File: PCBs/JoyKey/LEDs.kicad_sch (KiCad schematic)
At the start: 5 parts

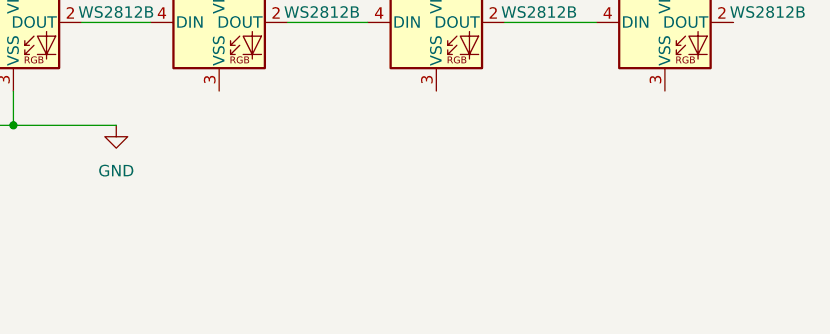
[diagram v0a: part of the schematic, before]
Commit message: Add draft schematics for all the input sources
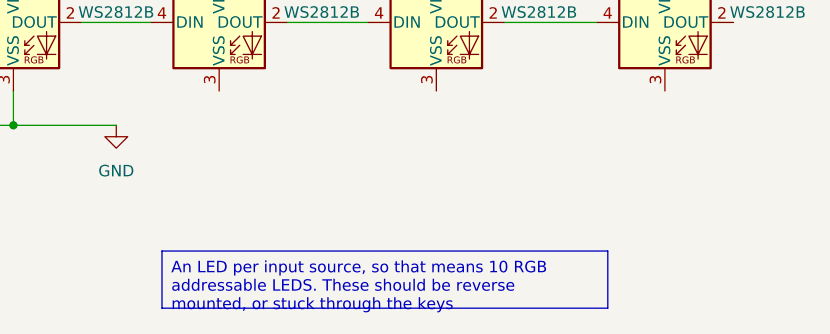
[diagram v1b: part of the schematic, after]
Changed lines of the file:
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@@
+		)
+	)
+	(text_box "An LED per input source, so that means 10 RGB addressable LEDS. These should be reverse mounted, or stuck through the keys"
+		(exclude_from_sim no)
+		(at 81.28 80.01 0)
+		(size 49.53 6.35)
+		(stroke
+			(width 0)
+			(type default)
+		)
+		(fill
+			(type none)
+		)
+		(effects
+			(font
+				(size 1.27 1.27)
+			)
+			(justify left top)
 		)
 	)

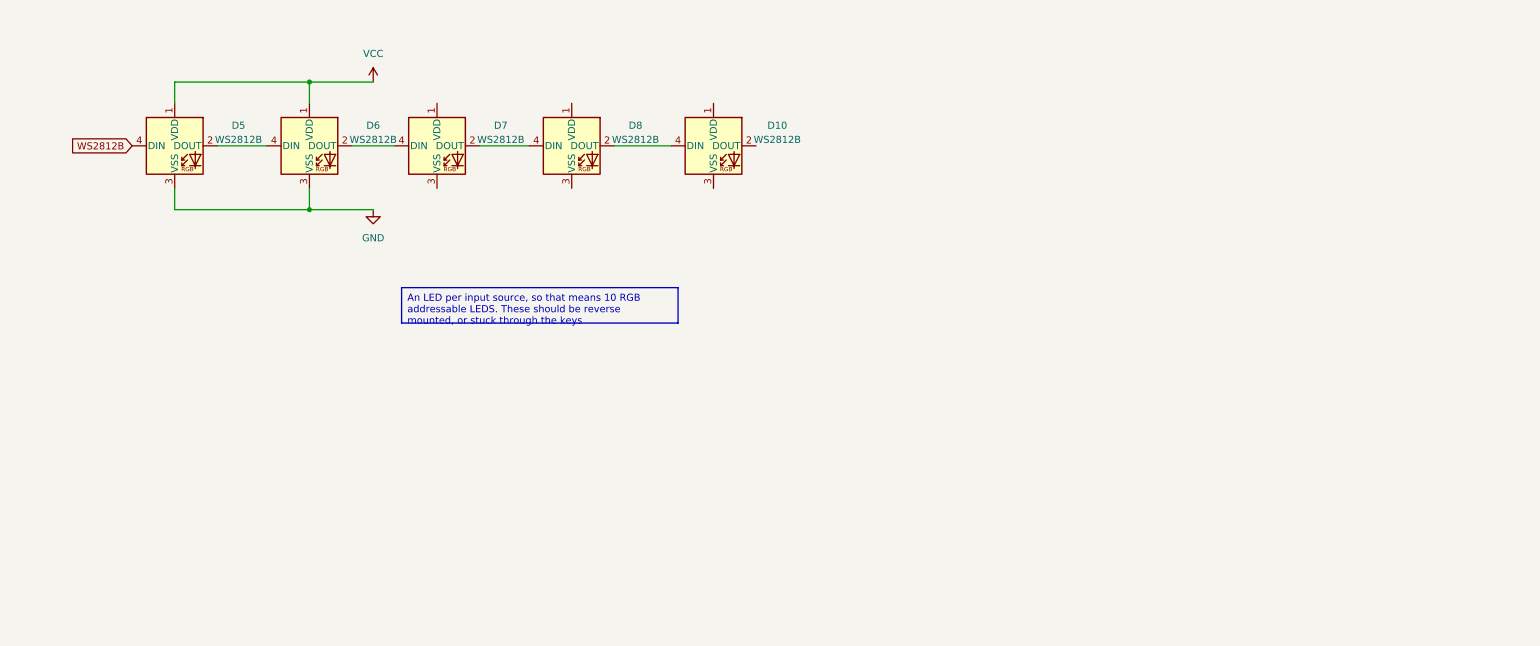
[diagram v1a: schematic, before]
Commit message: Rearranged LEDs and switched to SK6812 mini -e
These are reverse mount RGB LEDs that I think would be better to use than the ws2812 leds
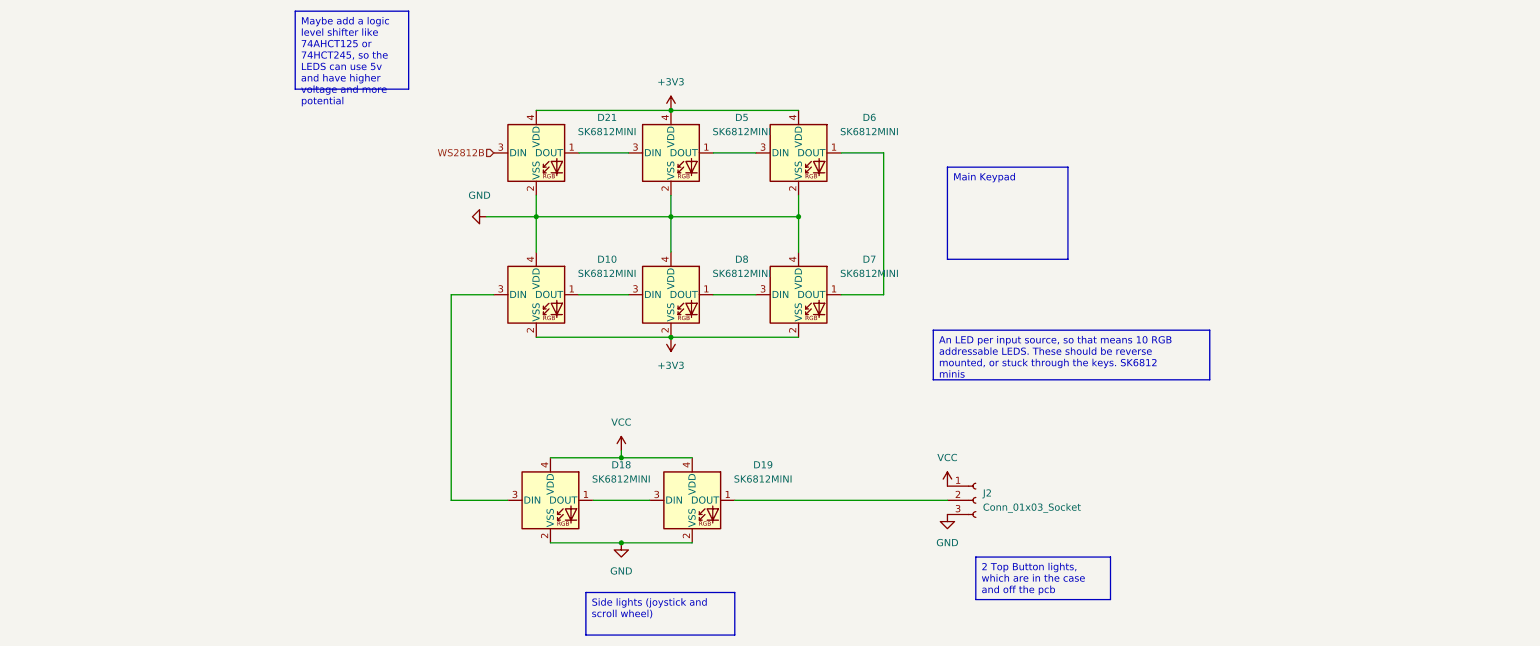
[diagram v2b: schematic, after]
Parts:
- removed D10, D5, D6, D7, D8: WS2812B, LED_SMD:LED_WS2812B_PLCC4_5.0x5.0mm_P3.2mm, symbol LED:WS2812B
- added D10, D18, D19, D21, D5, D6, D7, D8: SK6812MINI, SK6812MINI-E:SK6812MINI-E, symbol LED:SK6812MINI
- added J2: Conn_01x03_Socket, Connector_PinHeader_2.54mm:PinHeader_1x03_P2.54mm_Vertical, symbol Connector:Conn_01x03_Socket
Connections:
- net GND: now also D10.4 (VDD), D18.2 (VSS), D19.2 (VSS), D21.2 (VSS), D5.2 (VSS), D6.2 (VSS), D7.4 (VDD), D8.4 (VDD), J2.3 (Pin_3)
- net VCC: now also D18.4 (VDD), D19.4 (VDD), J2.1 (Pin_1)
- net WS2812B: now also D21.3 (DIN)
- new net: D21.1 (DOUT), D5.3 (DIN)
- new net: D18.1 (DOUT), D19.3 (DIN)
- new net: D10.3 (DIN), D18.3 (DIN)
- new net: D19.1 (DOUT), J2.2 (Pin_2)
- new net: D6.1 (DOUT), D7.1 (DOUT)
- new net: D5.1 (DOUT), D6.3 (DIN)
- new net: D7.3 (DIN), D8.1 (DOUT)
- new net: D10.1 (DOUT), D8.3 (DIN)
- new net +3V3: D10.2 (VSS), D21.4 (VDD), D5.4 (VDD), D6.4 (VDD), D7.2 (VSS), D8.2 (VSS)

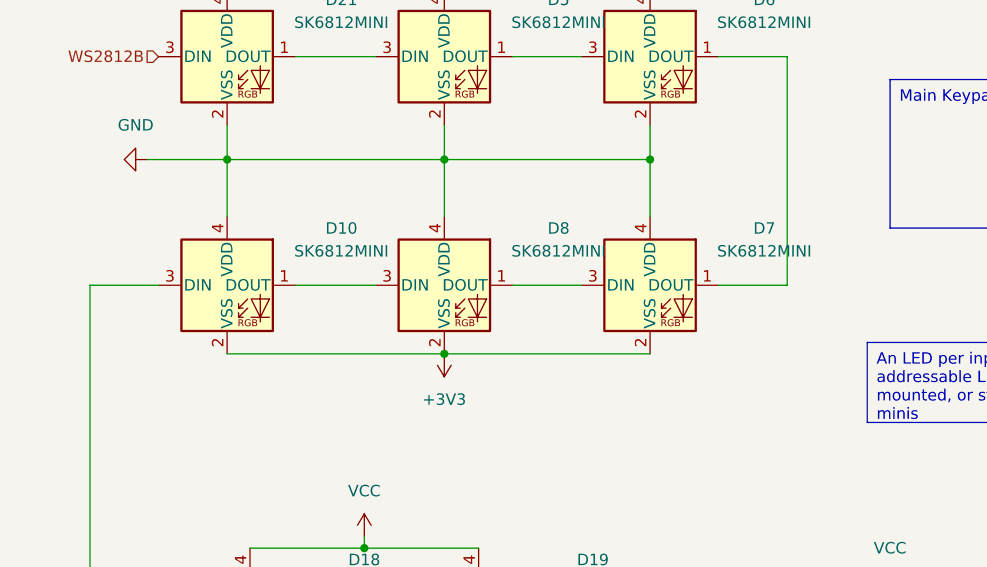
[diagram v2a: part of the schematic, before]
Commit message: Fixed bug w reverse orientation of LEDs
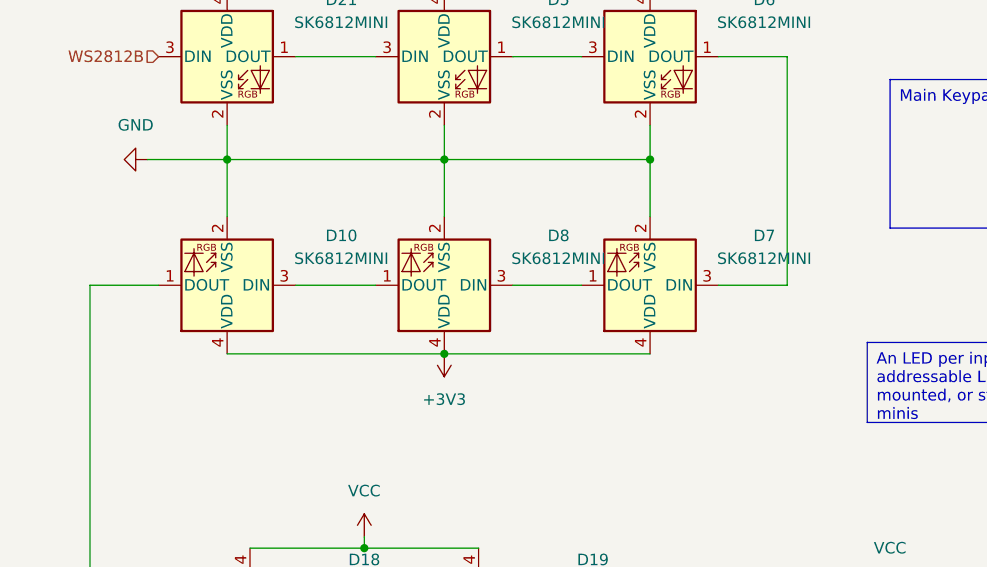
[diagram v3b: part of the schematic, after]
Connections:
- net +3V3: now also D10.4 (VDD), D7.4 (VDD), D8.4 (VDD); no longer D10.2 (VSS), D7.2 (VSS), D8.2 (VSS)
- net GND: now also D10.2 (VSS), D7.2 (VSS), D8.2 (VSS); no longer D10.4 (VDD), D7.4 (VDD), D8.4 (VDD)
- net at D18.3 (DIN): now also D10.1 (DOUT); no longer D10.3 (DIN)
- net at D6.1 (DOUT): now also D7.3 (DIN); no longer D7.1 (DOUT)
- net at D8.1 (DOUT): now also D10.3 (DIN); no longer D7.3 (DIN)
- net at D8.3 (DIN): now also D7.1 (DOUT); no longer D10.1 (DOUT)
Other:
- moved on the sheet: D10, D7, D8
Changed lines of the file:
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@@
 	(symbol
 		(lib_id "LED:SK6812MINI")
-		(at 129.54 81.28 0)
+		(at 129.54 81.28 180)
 		(unit 1)
 		(exclude_from_sim no)
@@
 		(fields_autoplaced yes)
 		(property "Reference" "D8"
-			(at 142.24 74.9614 0)
+			(at 142.24 75.7838 0)
 			(effects
 				(font
@@
 		)
 		(property "Value" "SK6812MINI"
-			(at 142.24 77.5014 0)
+			(at 142.24 78.3238 0)
 			(effects
 				(font
@@
 		)
 		(property "Footprint" "SK6812MINI-E:SK6812MINI-E"
-			(at 130.81 88.9 0)
+			(at 128.27 73.66 0)
 			(effects
 				(font
@@
 		)
 		(property "Datasheet" "https://cdn-shop.adafruit.com/product-files/2686/SK6812MINI_REV.01-1-2.pdf"
-			(at 132.08 90.805 0)
+			(at 127 71.755 0)
 			(effects
 				(font
@@
 	(symbol
 		(lib_id "LED:SK6812MINI")
-		(at 152.4 81.28 0)
+		(at 152.4 81.28 180)
 		(unit 1)
 		(exclude_from_sim no)
@@
 		(fields_autoplaced yes)
 		(property "Reference" "D7"
-			(at 165.1 74.9614 0)
+			(at 165.1 75.7838 0)
 			(effects
 				(font
@@
 		)
 		(property "Value" "SK6812MINI"
-			(at 165.1 77.5014 0)
+			(at 165.1 78.3238 0)
 			(effects
 				(font
@@
 		)
 		(property "Footprint" "SK6812MINI-E:SK6812MINI-E"
-			(at 153.67 88.9 0)
+			(at 151.13 73.66 0)
 			(effects
 				(font
@@
 		)
 		(property "Datasheet" "https://cdn-shop.adafruit.com/product-files/2686/SK6812MINI_REV.01-1-2.pdf"
-			(at 154.94 90.805 0)
+			(at 149.86 71.755 0)
 			(effects
 				(font
@@
 	(symbol
 		(lib_id "LED:SK6812MINI")
-		(at 105.41 81.28 0)
+		(at 105.41 81.28 180)
 		(unit 1)
 		(exclude_from_sim no)
@@
 		(fields_autoplaced yes)
 		(property "Reference" "D10"
-			(at 118.11 74.9614 0)
+			(at 118.11 75.7838 0)
 			(effects
 				(font
@@
 		)
 		(property "Value" "SK6812MINI"
-			(at 118.11 77.5014 0)
+			(at 118.11 78.3238 0)
 			(effects
 				(font
@@
 		)
 		(property "Footprint" "SK6812MINI-E:SK6812MINI-E"
-			(at 106.68 88.9 0)
+			(at 104.14 73.66 0)
 			(effects
 				(font
@@
 		)
 		(property "Datasheet" "https://cdn-shop.adafruit.com/product-files/2686/SK6812MINI_REV.01-1-2.pdf"
-			(at 107.95 90.805 0)
-			(effects
-				(font
+			(at 102.87 71.755 0)
+			(effects
+				(font

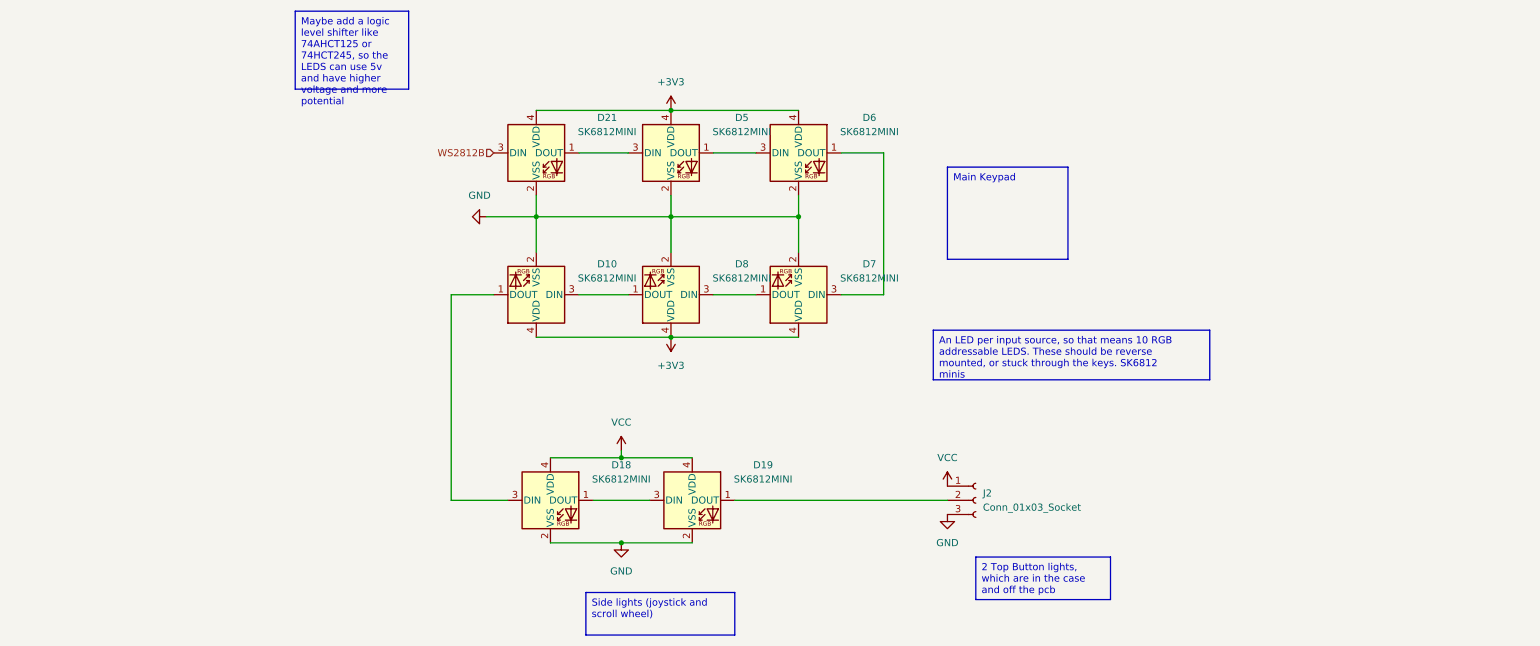
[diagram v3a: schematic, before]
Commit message: Updated to not distinguished btw LEDs per element
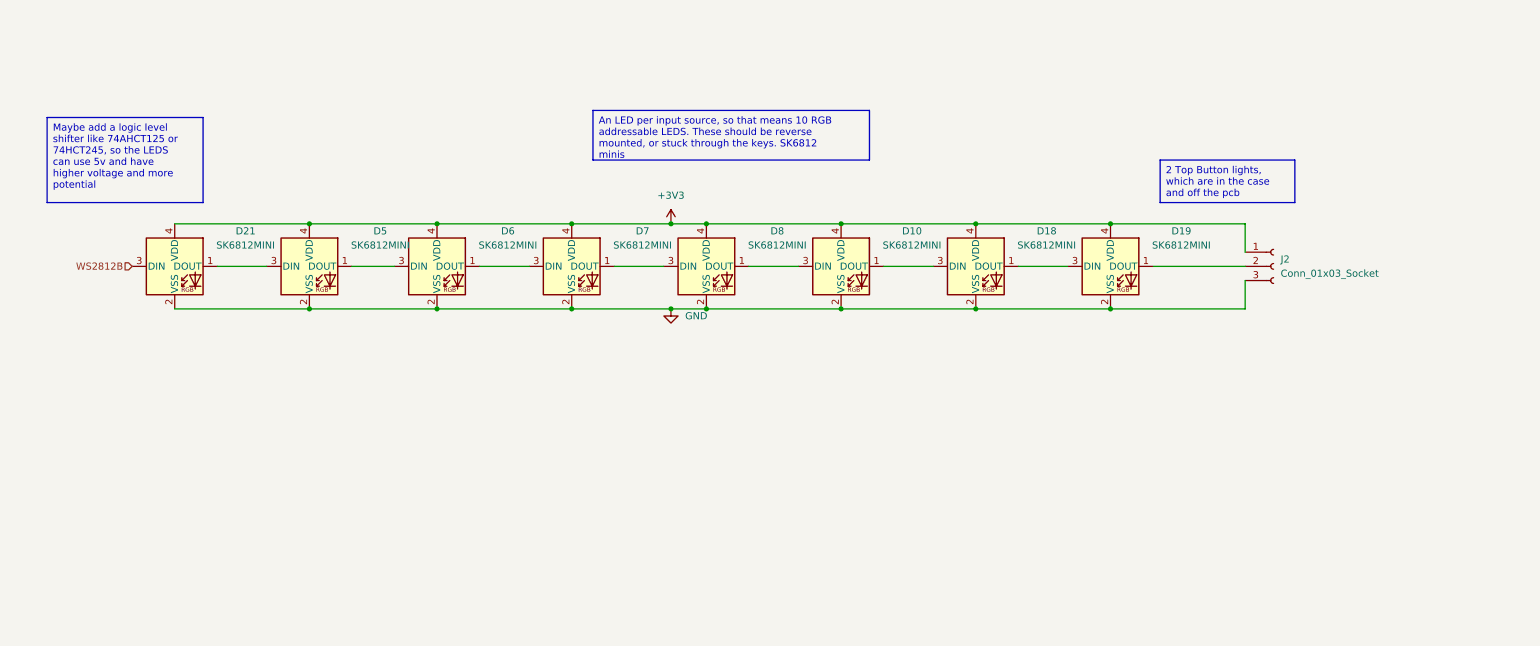
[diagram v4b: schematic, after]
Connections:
- net VCC is gone; now on net +3V3: D18.4 (VDD), D19.4 (VDD), J2.1 (Pin_1)
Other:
- moved on the sheet: D10, D18, D19, D21, D5, D6, D7, D8, J2

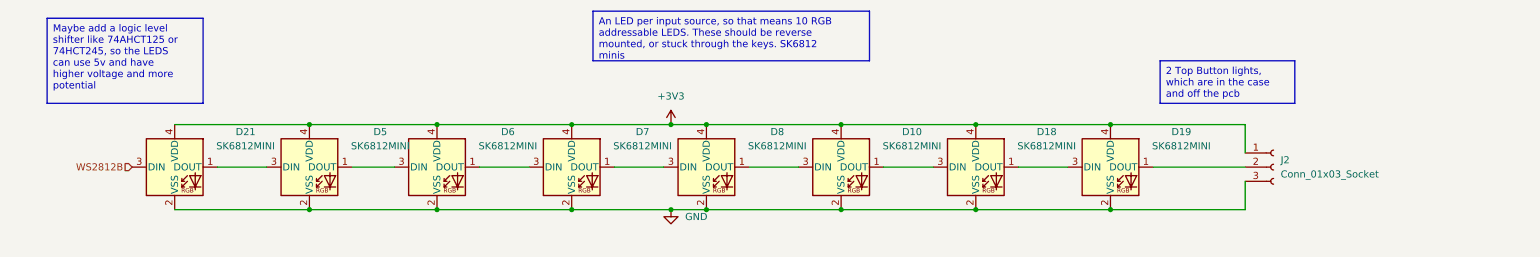
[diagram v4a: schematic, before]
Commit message: Added 2 extra LEDs
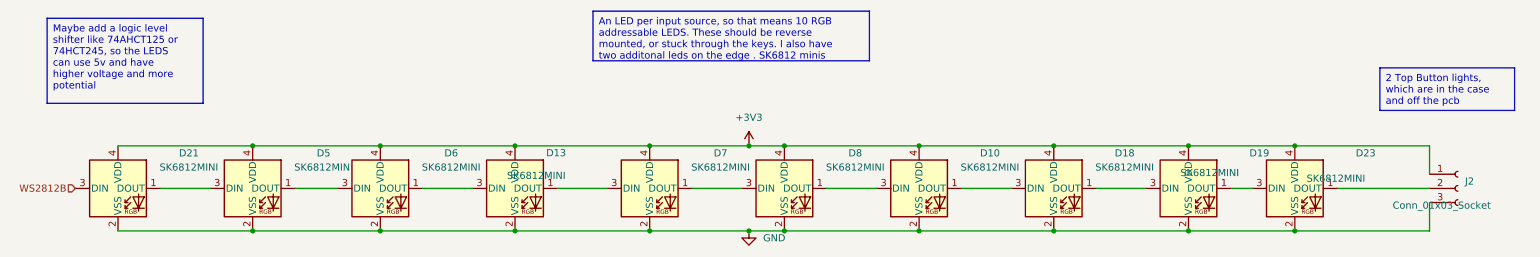
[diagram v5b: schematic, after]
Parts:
- added D13, D23: SK6812MINI, SK6812MINI-E:SK6812MINI-E, symbol LED:SK6812MINI
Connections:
- net +3V3: now also D13.4 (VDD), D23.4 (VDD)
- net GND: now also D13.2 (VSS), D23.2 (VSS)
- net at D19.1 (DOUT): now also D23.3 (DIN); no longer J2.2 (Pin_2)
- net at D6.1 (DOUT): now also D13.3 (DIN); no longer D7.3 (DIN)
- new net: D13.1 (DOUT), D7.3 (DIN)
- new net: D23.1 (DOUT), J2.2 (Pin_2)
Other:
- moved on the sheet: D10, D18, D19, D21, D5, D6, D7, D8, J2
